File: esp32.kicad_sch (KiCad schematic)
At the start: 20 parts, among them SW3 SW_Push, SW4 SW_Push, U7 ESP32-PICO-MINI-02-N8R2

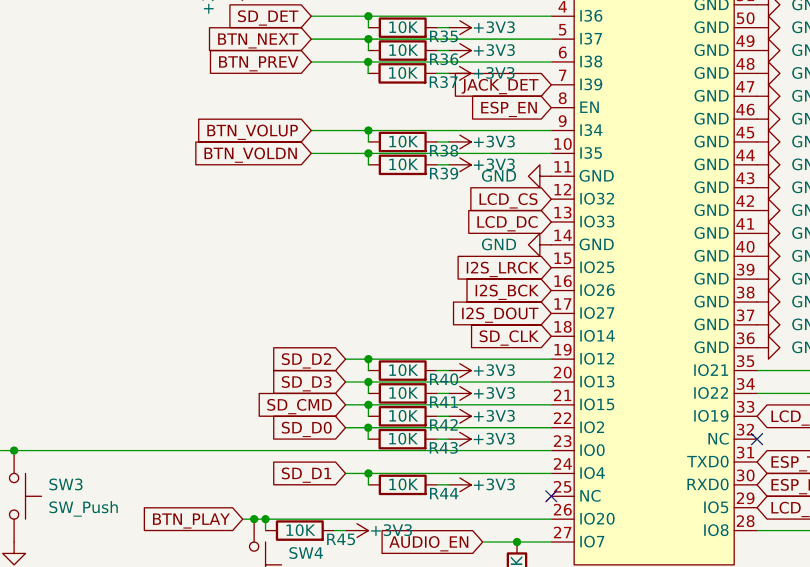
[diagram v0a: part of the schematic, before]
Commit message: Schematic: microSD, display and buttons sheet; drop ST7567
- microSD (TF-01A) with 33R on CLK and decoupling
- Sharp LS013B7DH03 on FH12-10S, DISP on IO33 (LCD_DISP, 100k pull-down,
  0.1uF per Sharp), EXTMODE/EXTCOMIN to GND
- VOL+/VOL-/NEXT/PREV buttons, jack detect (100k series + 1M pull-up)
- ST7567 removed: Sharp is the only display (same display across projects)

Co-Authored-By: Claude Opus 5.5 <noreply@anthropic.com>
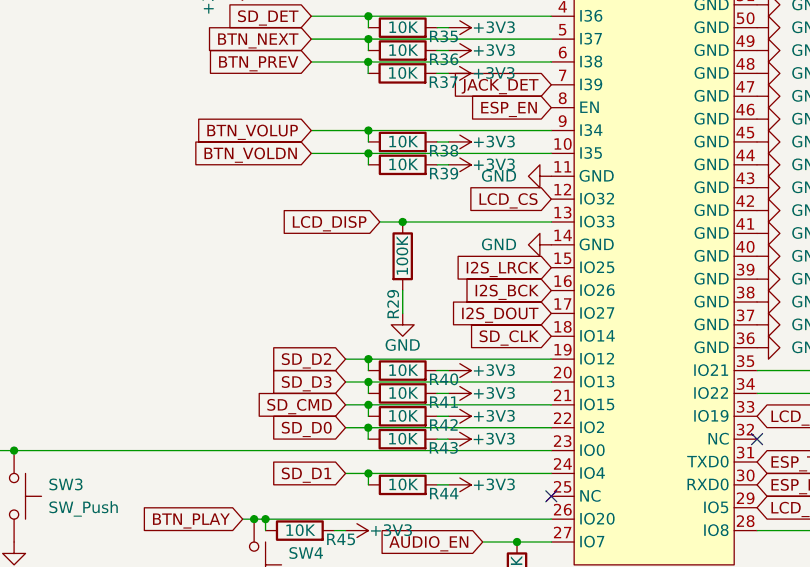
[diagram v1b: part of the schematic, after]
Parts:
- added R29: 100K, symbol Device:R
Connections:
- net GND: now also R29.2
- net LCD_DC renamed LCD_DISP
- net LCD_DISP: now also R29.1
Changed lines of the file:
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@@
 	)
 	(junction
+		(at 113.03 92.71)
+		(diameter 0)
+		(color 0 0 0 0)
+	)
+	(junction
 		(at 109.22 120.65)
 		(diameter 0)
@@
 	(wire
 		(pts
+			(xy 110.49 92.71) (xy 113.03 92.71)
+		)
+		(stroke
+			(width 0)
+			(type default)
+		)
+	)
+	(wire
+		(pts
 			(xy 99.06 59.69) (xy 96.52 59.69)
 		)
@@
 	(wire
 		(pts
+			(xy 113.03 92.71) (xy 129.54 92.71)
+		)
+		(stroke
+			(width 0)
+			(type default)
+		)
+	)
+	(wire
+		(pts
+			(xy 113.03 100.33) (xy 113.03 102.87)
+		)
+		(stroke
+			(width 0)
+			(type default)
+		)
+	)
+	(wire
+		(pts
 			(xy 118.11 86.36) (xy 116.84 86.36)
 		)
@@
 		)
 	)
-	(global_label "LCD_DC"
+	(global_label "LCD_DISP"
 		(shape input)
-		(at 129.54 92.71 180)
+		(at 110.49 92.71 180)
 		(fields_autoplaced yes)
 		(effects
@@
 		)
 		(property "Intersheetrefs" "${INTERSHEET_REFS}"
-			(at 119.4791 92.71 0)
+			(at 98.6148 92.71 0)
 			(hide yes)
 			(show_name no)
@@
 	(symbol
 		(lib_id "Device:R")
+		(at 113.03 96.52 0)
+		(unit 1)
+		(body_style 1)
+		(exclude_from_sim no)
+		(in_bom yes)
+		(on_board yes)
+		(in_pos_files yes)
+		(dnp no)
+		(property "Reference" "R29"
+			(at 112.014 101.854 90)
+			(show_name no)
+			(do_not_autoplace no)
+			(effects
+				(font
+					(size 1.27 1.27)
+				)
+			)
+		)
+		(property "Value" "100K"
+			(at 113.03 96.52 90)
+			(show_name no)
+			(do_not_autoplace no)
+			(effects
+				(font
+					(size 1.27 1.27)
+				)
+			)
+		)
+		(property "Footprint" ""
+			(at 111.252 96.52 90)
+			(hide yes)
+			(show_name no)
+			(do_not_autoplace no)
+			(effects
+				(font
+					(size 1.27 1.27)
+				)
+			)
+		)
+		(property "Datasheet" ""
+			(at 113.03 96.52 0)
+			(hide yes)
+			(show_name no)
+			(do_not_autoplace no)
+			(effects
+				(font
+					(size 1.27 1.27)
+				)
+			)
+		)
+		(property "Description" "Resistor"
+			(at 113.03 96.52 0)
+			(hide yes)
+			(show_name no)
+			(do_not_autoplace no)
+			(effects
+				(font
+					(size 1.27 1.27)
+				)
+			)
+		)
+		(pin "2"
+		)
+		(pin "1"
+		)
+		(instances
+			(project "mp3_player"
+				(path "/e7a6a6cd-6e47-432f-a794-94ecc7288598"
+					(reference "R29")
+					(unit 1)
+				)
+			)
+		)
+	)
+	(symbol
+		(lib_id "Device:R")
 		(at 113.03 71.12 90)
 		(unit 1)
@@
 					(unit 1)
 				)
+			)
+		)
+	)
+	(symbol
+		(lib_id "power:GND")
+		(at 113.03 102.87 0)
+		(unit 1)
+		(body_style 1)
+		(exclude_from_sim no)
+		(in_bom yes)
+		(on_board yes)
+		(in_pos_files yes)
+		(dnp no)
+		(property "Reference" "#PWR0128"
+			(at 113.03 109.22 0)
+			(hide yes)
+			(show_name no)
+			(do_not_autoplace no)
+			(effects
+				(font
+					(size 1.27 1.27)
+				)
+			)
+		)
+		(property "Value" "GND"
+			(at 113.03 106.426 0)
+			(show_name no)
+			(do_not_autoplace no)
+			(effects
+				(font
+					(size 1.27 1.27)
+				)
+			)
+		)
+		(property "Footprint" ""
+			(at 113.03 102.87 0)
+			(hide yes)
+			(show_name no)
+			(do_not_autoplace no)
+			(effects
+				(font
+					(size 1.27 1.27)
+				)
+			)
+		)
+		(property "Datasheet" ""
+			(at 113.03 102.87 0)
+			(hide yes)
+			(show_name no)
+			(do_not_autoplace no)
+			(effects
+				(font
+					(size 1.27 1.27)
+				)
+			)
+		)
+		(property "Description" "Power symbol creates a global label with name \"GND\" , ground"
+			(at 113.03 102.87 0)
+			(hide yes)
+			(show_name no)
+			(do_not_autoplace no)
+			(effects
+				(font
+					(size 1.27 1.27)
+				)
+			)
+		)
+		(pin "1"
+		)
+		(instances
+			(project "mp3_player"
+				(path "/e7a6a6cd-6e47-432f-a794-94ecc7288598"
+					(reference "#PWR0128")
+					(unit 1)
+				)

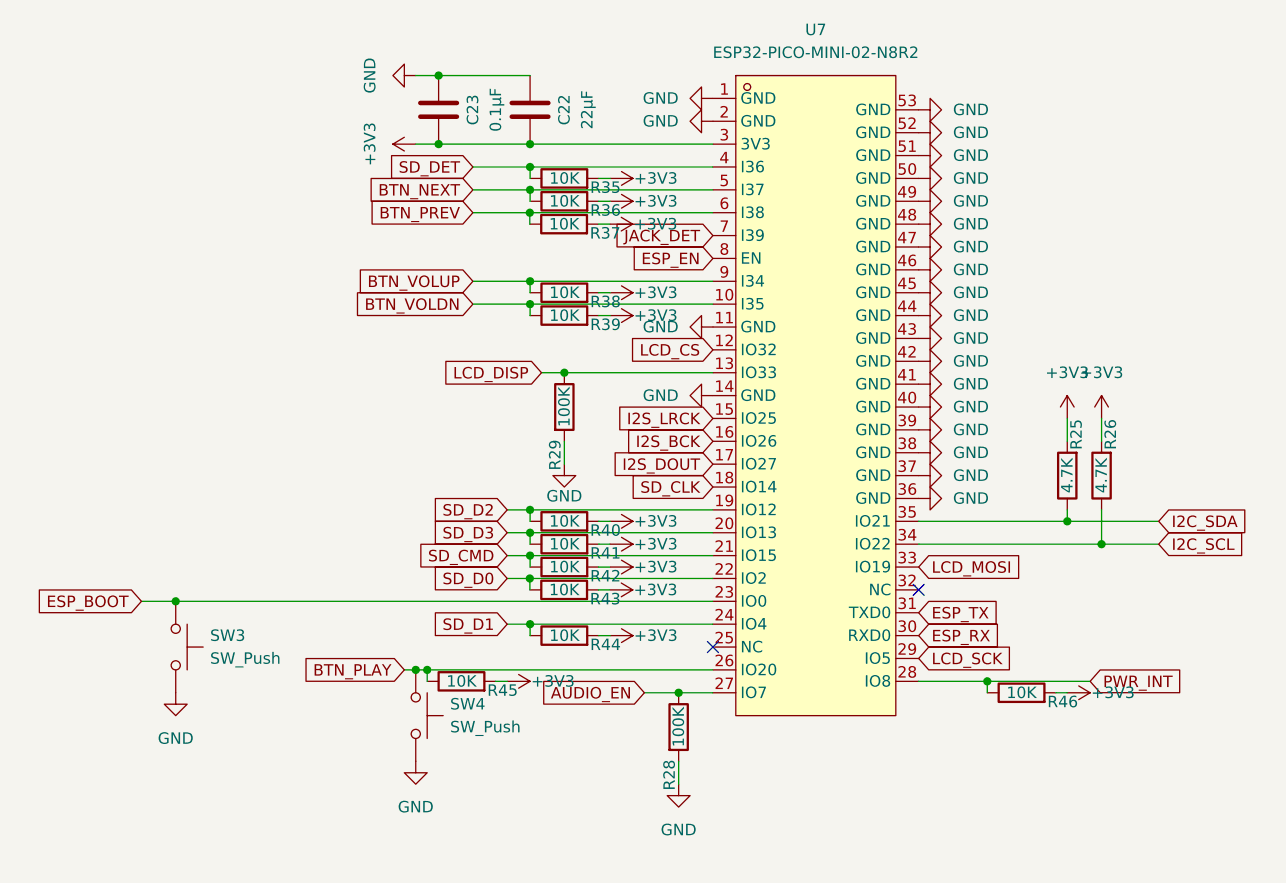
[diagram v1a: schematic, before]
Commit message: Schematic done
- sheet files renamed to English (usb, power, esp32, audio, io)
- final layout, annotation R1-R42 / C1-C43 / U1-U9 / J1-J4 / SW1-SW8
- all buttons are TS-1088, project R/C symbols, PWR_FLAGs
- connections.md replaces conexiuni.md (English, final references)
- final check on the KiCad netlist: 278/278 checks against connections.md
- status updated; firmware note: BQ25180 charge current defaults to ~10 mA

Co-Authored-By: Claude Opus 5.5 <noreply@anthropic.com>
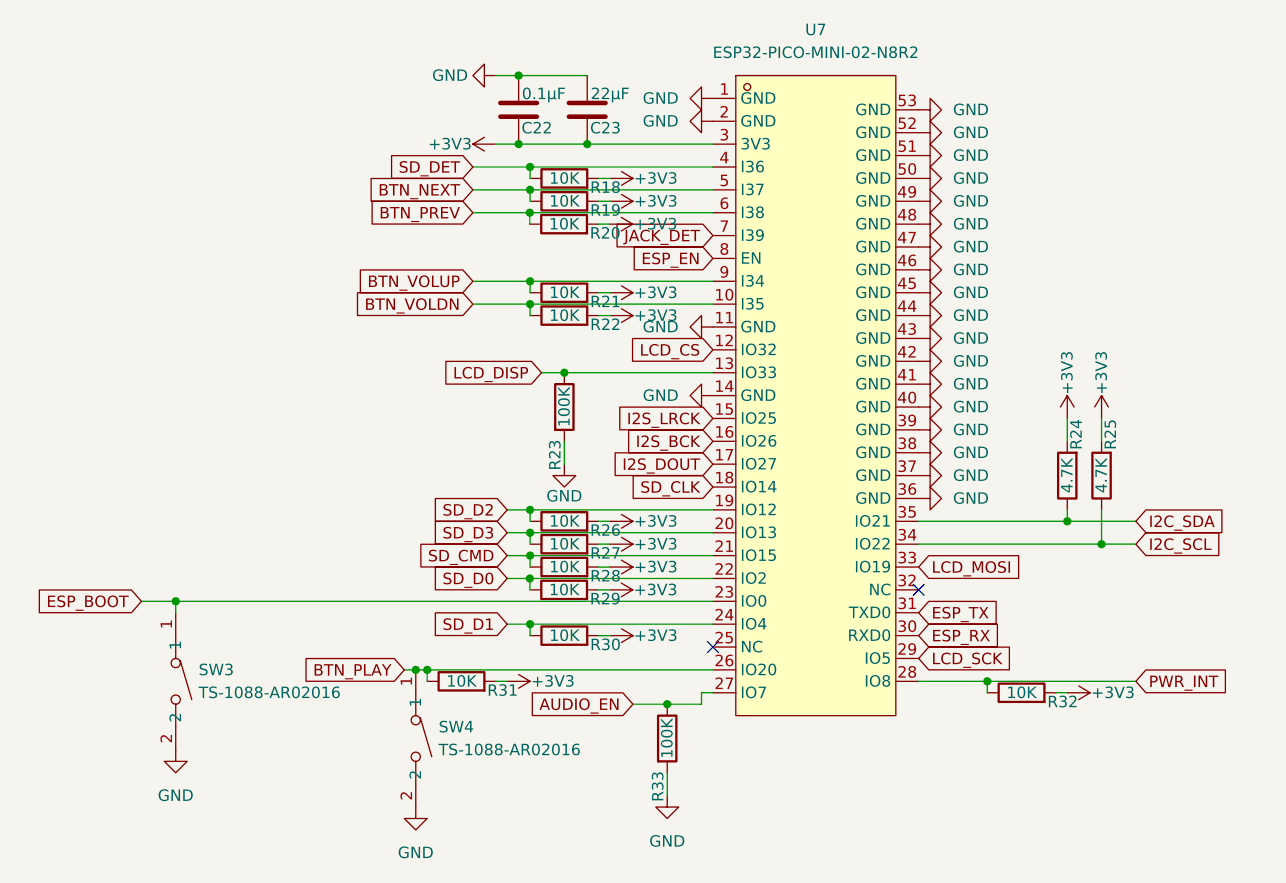
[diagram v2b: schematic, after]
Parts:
- removed SW3, SW4: SW_Push, symbol Switch:SW_Push
- added SW3, SW4: TS-1088-AR02016, mp3_player:SW-SMD_L3.9-W3.0-P4.45, symbol mp3_player:TS-1088-AR02016
- R18: renamed from R35; symbol Device:R -> mp3_player:R
- R19: renamed from R36; symbol Device:R -> mp3_player:R
- R20: renamed from R37; symbol Device:R -> mp3_player:R
- R21: renamed from R38; symbol Device:R -> mp3_player:R
- R22: renamed from R39; symbol Device:R -> mp3_player:R
- R23: renamed from R29; symbol Device:R -> mp3_player:R
- R24: renamed from R25; symbol Device:R -> mp3_player:R
- R25: renamed from R26; symbol Device:R -> mp3_player:R
- R26: renamed from R40; symbol Device:R -> mp3_player:R
- R27: renamed from R41; symbol Device:R -> mp3_player:R
- R28: renamed from R42; symbol Device:R -> mp3_player:R
- R29: renamed from R43; symbol Device:R -> mp3_player:R
- R30: renamed from R44; symbol Device:R -> mp3_player:R
- R31: renamed from R45; symbol Device:R -> mp3_player:R
- R32: renamed from R46; symbol Device:R -> mp3_player:R
- R33: renamed from R28; symbol Device:R -> mp3_player:R
- renumbered C23 to C22, C22 to C23
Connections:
- net BTN_PLAY: now also SW4.1
- net ESP_BOOT: now also SW3.1
- net GND: now also SW3.2, SW4.2
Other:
- moved on the sheet: C22, C23, R33

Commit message: Assign footprints and LCSC parts to passives, D2 and BT1
Thin-film 0.1% resistors in the audio path and rail dividers, C0G caps
in the DAC output filter, Samsung/Murata MLCCs with 0603/0805 cases for
bulk caps. Passive choices documented in mp3_player.md.

Co-Authored-By: Claude Opus 5.5 <noreply@anthropic.com>
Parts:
- C22: footprint (none) -> Capacitor_SMD:C_0402_1005Metric; LCSC Part (none) -> C1525
- C23: footprint (none) -> Capacitor_SMD:C_0805_2012Metric; LCSC Part (none) -> C45783
- R18, R19, R20, R21, R22, R26, R27, R28, R29, R30, R31, R32: footprint (none) -> Resistor_SMD:R_0402_1005Metric; LCSC Part (none) -> C190095
- R23, R33: footprint (none) -> Resistor_SMD:R_0402_1005Metric; LCSC Part (none) -> C852472
- R24, R25: footprint (none) -> Resistor_SMD:R_0402_1005Metric; LCSC Part (none) -> C25900
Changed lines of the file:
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@@
 			)
 		)
-		(property "Footprint" ""
+		(property "Footprint" "Resistor_SMD:R_0402_1005Metric"
+			(at 174.498 104.14 90)
+			(hide yes)
+			(show_name no)
+			(do_not_autoplace no)
+			(effects
+				(font
+					(size 1.27 1.27)
+				)
+			)
+		)
+				(property "LCSC Part" "C25900"
 			(at 174.498 104.14 90)
 			(hide yes)
@@
 			)
 		)
-		(property "Footprint" ""
+		(property "Footprint" "Resistor_SMD:R_0402_1005Metric"
+			(at 113.03 75.438 90)
+			(hide yes)
+			(show_name no)
+			(do_not_autoplace no)
+			(effects
+				(font
+					(size 1.27 1.27)
+				)
+			)
+		)
+				(property "LCSC Part" "C190095"
 			(at 113.03 75.438 90)
 			(hide yes)
@@
 			)
 		)
-		(property "Footprint" ""
+		(property "Footprint" "Resistor_SMD:R_0402_1005Metric"
+			(at 113.0073 118.618 90)
+			(hide yes)
+			(show_name no)
+			(do_not_autoplace no)
+			(effects
+				(font
+					(size 1.27 1.27)
+				)
+			)
+		)
+				(property "LCSC Part" "C190095"
 			(at 113.0073 118.618 90)
 			(hide yes)
@@
 			)
 		)
-		(property "Footprint" ""
+		(property "Footprint" "Resistor_SMD:R_0402_1005Metric"
+			(at 111.252 96.52 90)
+			(hide yes)
+			(show_name no)
+			(do_not_autoplace no)
+			(effects
+				(font
+					(size 1.27 1.27)
+				)
+			)
+		)
+				(property "LCSC Part" "C852472"
 			(at 111.252 96.52 90)
 			(hide yes)
@@
 			)
 		)
-		(property "Footprint" ""
+		(property "Footprint" "Resistor_SMD:R_0402_1005Metric"
+			(at 113.03 72.898 90)
+			(hide yes)
+			(show_name no)
+			(do_not_autoplace no)
+			(effects
+				(font
+					(size 1.27 1.27)
+				)
+			)
+		)
+				(property "LCSC Part" "C190095"
 			(at 113.03 72.898 90)
 			(hide yes)
@@
 			)
 		)
-		(property "Footprint" ""
+		(property "Footprint" "Resistor_SMD:R_0402_1005Metric"
+			(at 113.03 116.078 90)
+			(hide yes)
+			(show_name no)
+			(do_not_autoplace no)
+			(effects
+				(font
+					(size 1.27 1.27)
+				)
+			)
+		)
+				(property "LCSC Part" "C190095"
 			(at 113.03 116.078 90)
 			(hide yes)
@@
 			)
 		)
-		(property "Footprint" ""
+		(property "Footprint" "Resistor_SMD:R_0402_1005Metric"
+			(at 122.682 133.35 90)
+			(hide yes)
+			(show_name no)
+			(do_not_autoplace no)
+			(effects
+				(font
+					(size 1.27 1.27)
+				)
+			)
+		)
+				(property "LCSC Part" "C852472"
 			(at 122.682 133.35 90)
 			(hide yes)
@@
 			)
 		)
-		(property "Footprint" ""
+		(property "Footprint" "Resistor_SMD:R_0402_1005Metric"
+			(at 113.03 113.538 90)
+			(hide yes)
+			(show_name no)
+			(do_not_autoplace no)
+			(effects
+				(font
+					(size 1.27 1.27)
+				)
+			)
+		)
+				(property "LCSC Part" "C190095"
 			(at 113.03 113.538 90)
 			(hide yes)
@@
 			)
 		)
-		(property "Footprint" ""
+		(property "Footprint" "Capacitor_SMD:C_0402_1005Metric"
+			(at 106.9848 59.69 0)
+			(hide yes)
+			(show_name no)
+			(do_not_autoplace no)
+			(effects
+				(font
+					(size 1.27 1.27)
+				)
+			)
+		)
+				(property "LCSC Part" "C1525"
 			(at 106.9848 59.69 0)
 			(hide yes)
@@
 			)
 		)
-		(property "Footprint" ""
+		(property "Footprint" "Resistor_SMD:R_0402_1005Metric"
+			(at 113.03 123.698 90)
+			(hide yes)
+			(show_name no)
+			(do_not_autoplace no)
+			(effects
+				(font
+					(size 1.27 1.27)
+				)
+			)
+		)
+				(property "LCSC Part" "C190095"
 			(at 113.03 123.698 90)
 			(hide yes)
@@
 			)
 		)
-		(property "Footprint" ""
+		(property "Footprint" "Resistor_SMD:R_0402_1005Metric"
+			(at 170.688 104.14 90)
+			(hide yes)
+			(show_name no)
+			(do_not_autoplace no)
+			(effects
+				(font
+					(size 1.27 1.27)
+				)
+			)
+		)
+				(property "LCSC Part" "C25900"
 			(at 170.688 104.14 90)
 			(hide yes)
@@
 			)
 		)
-		(property "Footprint" ""
+		(property "Footprint" "Resistor_SMD:R_0402_1005Metric"
+			(at 113.03 88.138 90)
+			(hide yes)
+			(show_name no)
+			(do_not_autoplace no)
+			(effects
+				(font
+					(size 1.27 1.27)
+				)
+			)
+		)
+				(property "LCSC Part" "C190095"
 			(at 113.03 88.138 90)
 			(hide yes)
@@
 			)
 		)
-		(property "Footprint" ""
+		(property "Footprint" "Capacitor_SMD:C_0805_2012Metric"
+			(at 114.6048 59.69 0)
+			(hide yes)
+			(show_name no)
+			(do_not_autoplace no)
+			(effects
+				(font
+					(size 1.27 1.27)
+				)
+			)
+		)
+				(property "LCSC Part" "C45783"
 			(at 114.6048 59.69 0)
 			(hide yes)
@@
 			)
 		)
-		(property "Footprint" ""
+		(property "Footprint" "Resistor_SMD:R_0402_1005Metric"
+			(at 163.83 130.048 90)
+			(hide yes)
+			(show_name no)
+			(do_not_autoplace no)
+			(effects
+				(font
+					(size 1.27 1.27)
+				)
+			)
+		)
+				(property "LCSC Part" "C190095"
 			(at 163.83 130.048 90)
 			(hide yes)
@@
 			)
 		)
-		(property "Footprint" ""
+		(property "Footprint" "Resistor_SMD:R_0402_1005Metric"
+			(at 113.0009 77.978 90)
+			(hide yes)
+			(show_name no)
+			(do_not_autoplace no)
+			(effects
+				(font
+					(size 1.27 1.27)
+				)
+			)
+		)
+				(property "LCSC Part" "C190095"
 			(at 113.0009 77.978 90)
 			(hide yes)
@@
 			)
 		)
-		(property "Footprint" ""
+		(property "Footprint" "Resistor_SMD:R_0402_1005Metric"
+			(at 113.03 85.598 90)
+			(hide yes)
+			(show_name no)
+			(do_not_autoplace no)
+			(effects
+				(font
+					(size 1.27 1.27)
+				)
+			)
+		)
+				(property "LCSC Part" "C190095"
 			(at 113.03 85.598 90)
 			(hide yes)
@@
 			)
 		)
-		(property "Footprint" ""
+		(property "Footprint" "Resistor_SMD:R_0402_1005Metric"
+			(at 113.027 110.998 90)
+			(hide yes)
+			(show_name no)
+			(do_not_autoplace no)
+			(effects
+				(font
+					(size 1.27 1.27)
+				)
+			)
+		)
+				(property "LCSC Part" "C190095"
 			(at 113.027 110.998 90)
 			(hide yes)
@@
 			)
 		)
-		(property "Footprint" ""
+		(property "Footprint" "Resistor_SMD:R_0402_1005Metric"
+			(at 101.6 128.778 90)
+			(hide yes)
+			(show_name no)
+			(do_not_autoplace no)
+			(effects
+				(font
+					(size 1.27 1.27)
+				)
+			)
+		)
+				(property "LCSC Part" "C190095"
 			(at 101.6 128.778 90)
 			(hide yes)
